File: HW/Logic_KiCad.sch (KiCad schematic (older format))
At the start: 32 parts, among them Q10 Q_NMOS_GSD, Q11 Q_NMOS_GSD, Q3 Q_NMOS_GSD, SW1 SW_SPDT, SW13 SW_SPST, SW14 SW_SPST, SW15 SW_SPST, U1 ESP32-PICO-D4

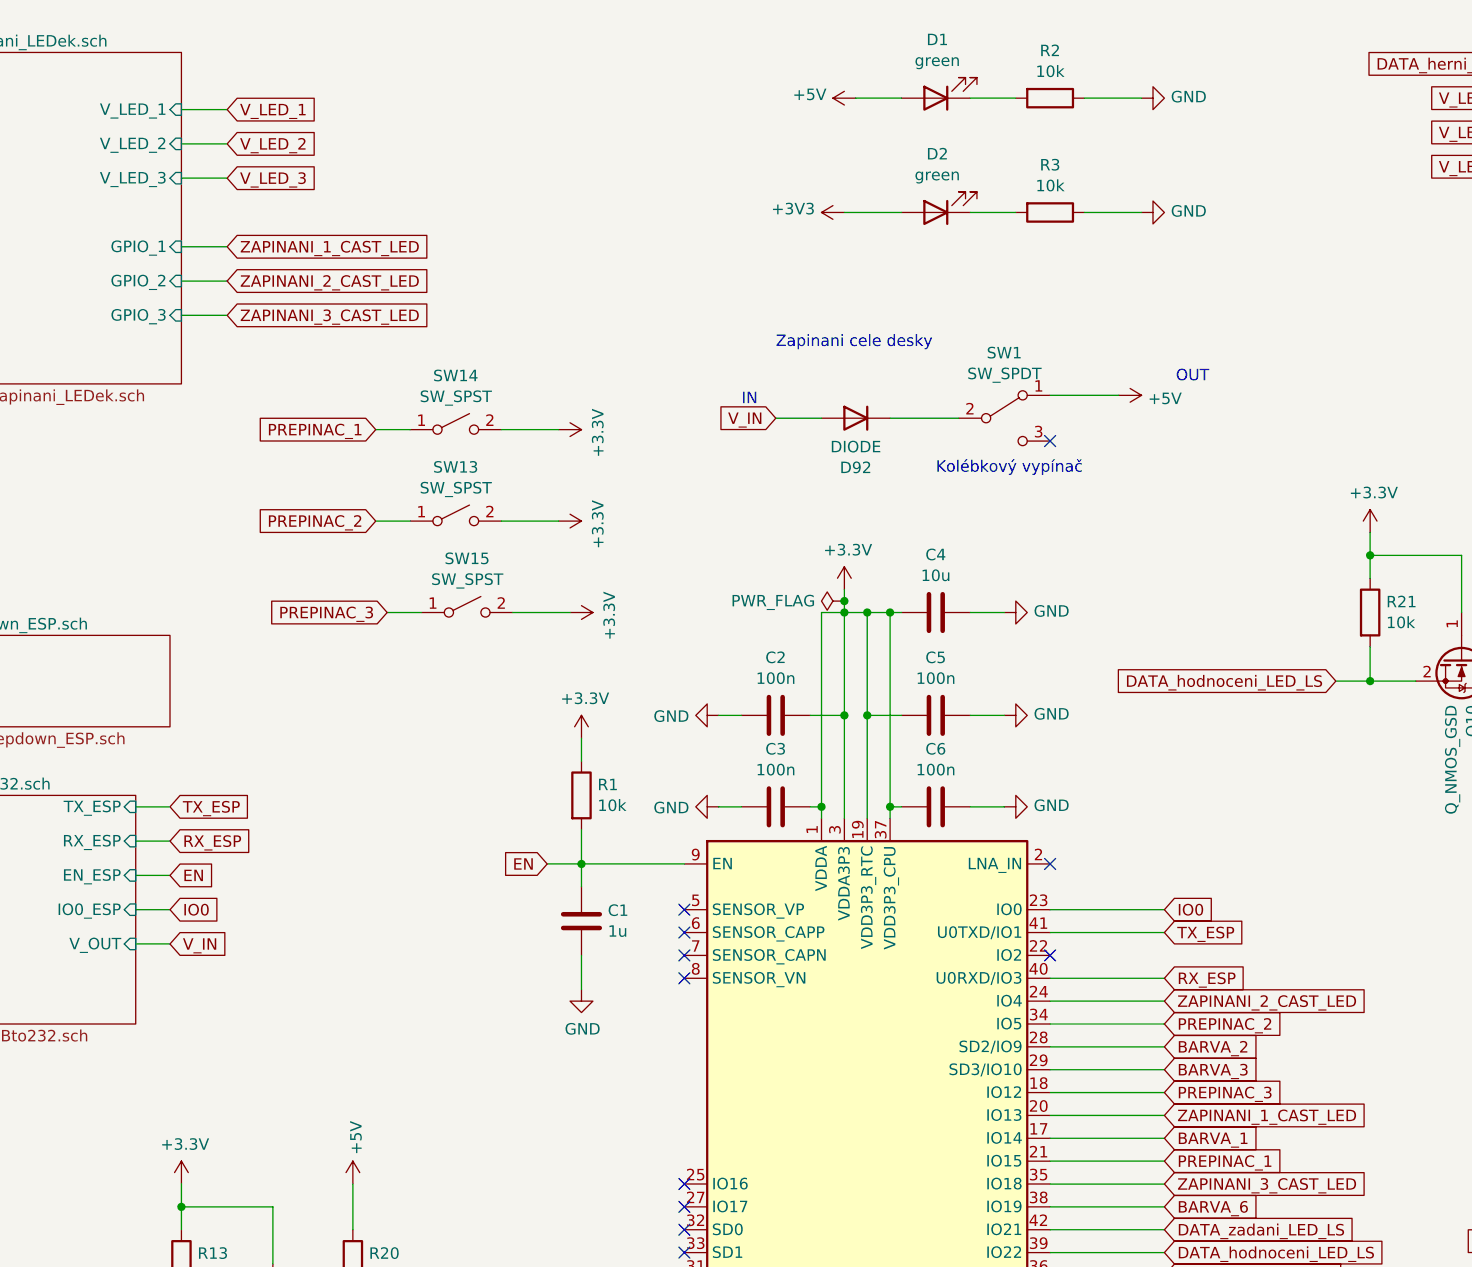
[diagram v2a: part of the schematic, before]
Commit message: repair DIPs, add pullup and pulldown resistors
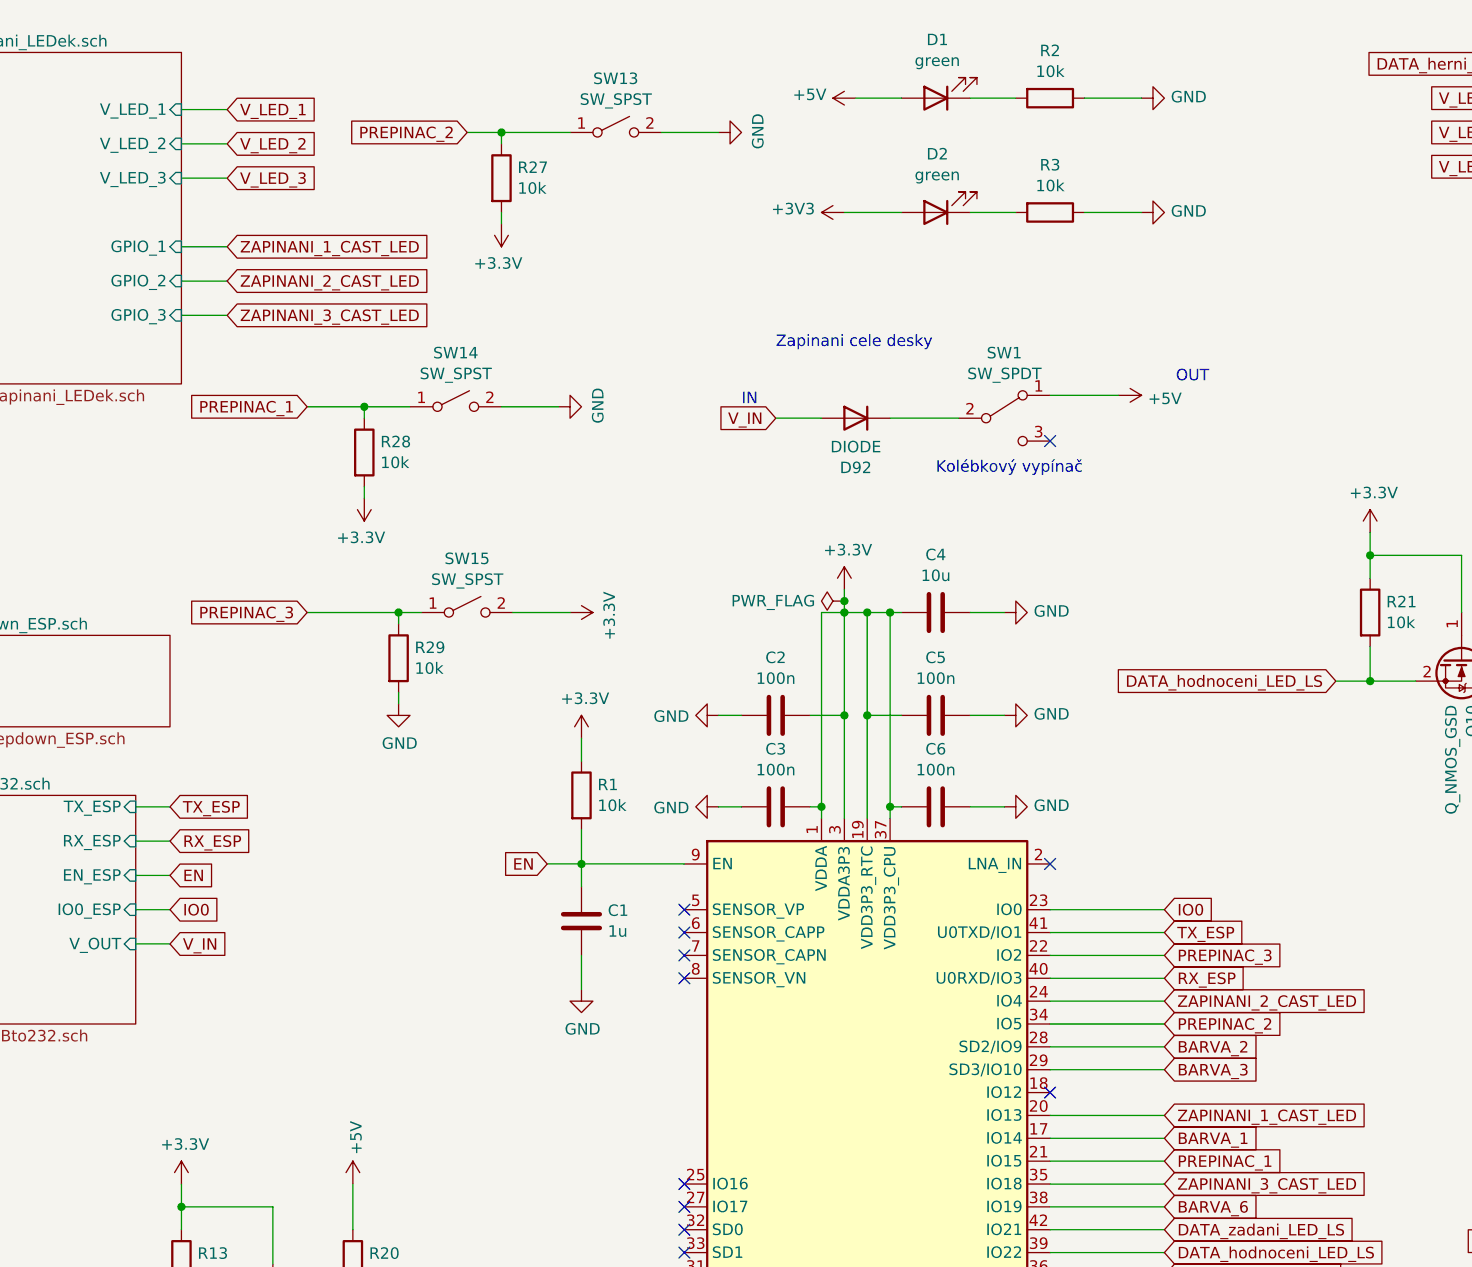
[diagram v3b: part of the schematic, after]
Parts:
- added R27, R28, R29: 10k, Resistor_SMD:R_0402_1005Metric, symbol Device:R
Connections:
- net +3V3: now also R27.2, R28.2; no longer SW13.2 (B), SW14.2 (B)
- net GND: now also SW13.2 (B), SW14.2 (B), R29.2
- net PREPINAC_1: now also R28.1
- net PREPINAC_2: now also R27.1
- net PREPINAC_3: now also U1.22 (IO2), R29.1; no longer U1.18 (IO12)
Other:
- moved on the sheet: SW13, SW14
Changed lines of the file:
@@
 L Switch:SW_SPST SW13
 U 1 1 603F7020
-P 2850 2750
-F 0 "SW13" H 2850 2985 50  0000 C CNN
-F 1 "SW_SPST" H 2850 2894 50  0000 C CNN
-F 2 "my_library:DIP1x1" H 2850 2750 50  0001 C CNN
-F 3 "~" H 2850 2750 50  0001 C CNN
-F 4 "0;0;0" H 2850 2750 50  0001 C CNN "JLCPCB_CORRECTION"
-F 5 "C54948" H 2850 2750 50  0001 C CNN "LCSC"
-	1    2850 2750
-	1    0    0    -1
-$EndComp
-Text GLabel 2500 2750 0    50   Input ~ 0
+P 3550 1050
+F 0 "SW13" H 3550 1285 50  0000 C CNN
+F 1 "SW_SPST" H 3550 1194 50  0000 C CNN
+F 2 "my_library:DIP1x1" H 3550 1050 50  0001 C CNN
+F 3 "~" H 3550 1050 50  0001 C CNN
+F 4 "0;0;0" H 3550 1050 50  0001 C CNN "JLCPCB_CORRECTION"
+F 5 "C54948" H 3550 1050 50  0001 C CNN "LCSC"
+	1    3550 1050
+	1    0    0    -1
+$EndComp
+Text GLabel 2900 1050 0    50   Input ~ 0
 PREPINAC_2
 Wire Wire Line
-	2650 2750 2500 2750
-Wire Wire Line
-	3300 2750 3050 2750
+	3350 1050 3050 1050
+Wire Wire Line
+	4000 1050 3750 1050
 $Comp
 L Switch:SW_SPST SW14
 U 1 1 604089F0
-P 2850 2350
-F 0 "SW14" H 2850 2585 50  0000 C CNN
-F 1 "SW_SPST" H 2850 2494 50  0000 C CNN
-F 2 "my_library:DIP1x1" H 2850 2350 50  0001 C CNN
-F 3 "~" H 2850 2350 50  0001 C CNN
-F 4 "0;0;0" H 2850 2350 50  0001 C CNN "JLCPCB_CORRECTION"
-F 5 "C54948" H 2850 2350 50  0001 C CNN "LCSC"
-	1    2850 2350
-	1    0    0    -1
-$EndComp
-Text GLabel 2500 2350 0    50   Input ~ 0
+P 2850 2250
+F 0 "SW14" H 2850 2485 50  0000 C CNN
+F 1 "SW_SPST" H 2850 2394 50  0000 C CNN
+F 2 "my_library:DIP1x1" H 2850 2250 50  0001 C CNN
+F 3 "~" H 2850 2250 50  0001 C CNN
+F 4 "0;0;0" H 2850 2250 50  0001 C CNN "JLCPCB_CORRECTION"
+F 5 "C54948" H 2850 2250 50  0001 C CNN "LCSC"
+	1    2850 2250
+	1    0    0    -1
+$EndComp
+Text GLabel 2200 2250 0    50   Input ~ 0
 PREPINAC_1
 Wire Wire Line
-	2650 2350 2500 2350
-Wire Wire Line
-	3300 2350 3050 2350
+	2650 2250 2450 2250
+Wire Wire Line
+	3300 2250 3050 2250
 Text GLabel 5950 4950 2    50   Input ~ 0
 PREPINAC_2
@@
 Wire Wire Line
 	5950 5550 5450 5550
-NoConn ~ 5450 4650
 Wire Wire Line
 	5950 4950 5450 4950
@@
 L power:+3.3V #PWR0224
 U 1 1 605155D5
-P 3300 2750
-F 0 "#PWR0224" H 3300 2600 50  0001 C CNN
-F 1 "+3.3V" H 3315 2923 50  0000 C CNN
-F 2 "" H 3300 2750 50  0001 C CNN
-F 3 "" H 3300 2750 50  0001 C CNN
-	1    3300 2750
-	0    1    1    0
-$EndComp
-Text GLabel 5950 5250 2    50   Input ~ 0
+P 3050 1450
+F 0 "#PWR0224" H 3050 1300 50  0001 C CNN
+F 1 "+3.3V" H 3065 1623 50  0000 C CNN
+F 2 "" H 3050 1450 50  0001 C CNN
+F 3 "" H 3050 1450 50  0001 C CNN
+	1    3050 1450
+	-1   0    0    1
+$EndComp
+Text GLabel 5950 4650 2    50   Input ~ 0
 PREPINAC_3
-Wire Wire Line
-	5450 5250 5950 5250
 $Comp
 L Switch:SW_SPST SW15
@@
 	1    0    0    -1
 $EndComp
-Text GLabel 2550 3150 0    50   Input ~ 0
+Text GLabel 2200 3150 0    50   Input ~ 0
 PREPINAC_3
 Wire Wire Line
-	2700 3150 2550 3150
+	2700 3150 2600 3150
 Wire Wire Line
 	3350 3150 3100 3150
@@
 L power:+3.3V #PWR0229
 U 1 1 6052B776
-P 3300 2350
-F 0 "#PWR0229" H 3300 2200 50  0001 C CNN
-F 1 "+3.3V" H 3315 2523 50  0000 C CNN
-F 2 "" H 3300 2350 50  0001 C CNN
-F 3 "" H 3300 2350 50  0001 C CNN
-	1    3300 2350
-	0    1    1    0
-$EndComp
+P 2450 2650
+F 0 "#PWR0229" H 2450 2500 50  0001 C CNN
+F 1 "+3.3V" H 2465 2823 50  0000 C CNN
+F 2 "" H 2450 2650 50  0001 C CNN
+F 3 "" H 2450 2650 50  0001 C CNN
+	1    2450 2650
+	-1   0    0    1
+$EndComp
+Wire Wire Line
+	5950 4650 5450 4650
+NoConn ~ 5450 5250
+$Comp
+L Device:R R28
+U 1 1 605389EB
+P 2450 2450
+F 0 "R28" H 2520 2496 50  0000 L CNN
+F 1 "10k" H 2520 2405 50  0000 L CNN
+F 2 "Resistor_SMD:R_0402_1005Metric" V 2380 2450 50  0001 C CNN
+F 3 "~" H 2450 2450 50  0001 C CNN
+F 4 "C25744" H 2450 2450 50  0001 C CNN "LCSC"
+F 5 "0;0;0" H 2450 2450 50  0001 C CNN "JLCPCB_CORRECTION"
+	1    2450 2450
+	1    0    0    -1
+$EndComp
+$Comp
+L Device:R R27
+U 1 1 60538DAC
+P 3050 1250
+F 0 "R27" H 3120 1296 50  0000 L CNN
+F 1 "10k" H 3120 1205 50  0000 L CNN
+F 2 "Resistor_SMD:R_0402_1005Metric" V 2980 1250 50  0001 C CNN
+F 3 "~" H 3050 1250 50  0001 C CNN
+F 4 "C25744" H 3050 1250 50  0001 C CNN "LCSC"
+F 5 "0;0;0" H 3050 1250 50  0001 C CNN "JLCPCB_CORRECTION"
+	1    3050 1250
+	1    0    0    -1
+$EndComp
+$Comp
+L Device:R R29
+U 1 1 605393EC
+P 2600 3350
+F 0 "R29" H 2670 3396 50  0000 L CNN
+F 1 "10k" H 2670 3305 50  0000 L CNN
+F 2 "Resistor_SMD:R_0402_1005Metric" V 2530 3350 50  0001 C CNN
+F 3 "~" H 2600 3350 50  0001 C CNN
+F 4 "C25744" H 2600 3350 50  0001 C CNN "LCSC"
+F 5 "0;0;0" H 2600 3350 50  0001 C CNN "JLCPCB_CORRECTION"
+	1    2600 3350
+	1    0    0    -1
+$EndComp
+$Comp
+L power:GND #PWR0230
+U 1 1 605398F0
+P 2600 3550
+F 0 "#PWR0230" H 2600 3300 50  0001 C CNN
+F 1 "GND" H 2605 3377 50  0000 C CNN
+F 2 "" H 2600 3550 50  0001 C CNN
+F 3 "" H 2600 3550 50  0001 C CNN
+	1    2600 3550
+	1    0    0    -1
+$EndComp
+$Comp
+L power:GND #PWR0231
+U 1 1 60539D13
+P 4000 1050
+F 0 "#PWR0231" H 4000 800 50  0001 C CNN
+F 1 "GND" H 4005 877 50  0000 C CNN
+F 2 "" H 4000 1050 50  0001 C CNN
+F 3 "" H 4000 1050 50  0001 C CNN
+	1    4000 1050
+	0    -1   -1   0
+$EndComp
+$Comp
+L power:GND #PWR0232
+U 1 1 60539F1B
+P 3300 2250
+F 0 "#PWR0232" H 3300 2000 50  0001 C CNN
+F 1 "GND" H 3305 2077 50  0000 C CNN
+F 2 "" H 3300 2250 50  0001 C CNN
+F 3 "" H 3300 2250 50  0001 C CNN
+	1    3300 2250
+	0    -1   -1   0
+$EndComp
+Wire Wire Line
+	2450 2300 2450 2250
+Connection ~ 2450 2250
+Wire Wire Line
+	2450 2250 2200 2250
+Wire Wire Line
+	3050 1100 3050 1050
+Connection ~ 3050 1050
+Wire Wire Line
+	3050 1050 2900 1050
+Wire Wire Line
+	2600 3200 2600 3150
+Connection ~ 2600 3150
+Wire Wire Line
+	2600 3150 2200 3150
+Wire Wire Line
+	2600 3500 2600 3550
+Wire Wire Line
+	3050 1450 3050 1400
+Wire Wire Line
+	2450 2650 2450 2600
 $EndSCHEMATC

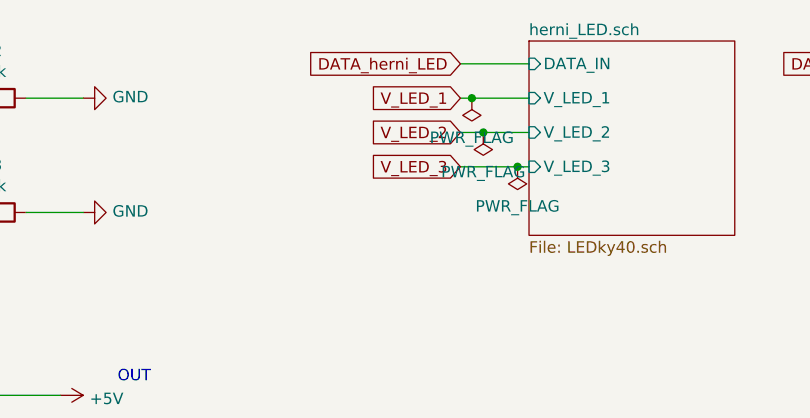
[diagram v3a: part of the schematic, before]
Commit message: add tooling holes
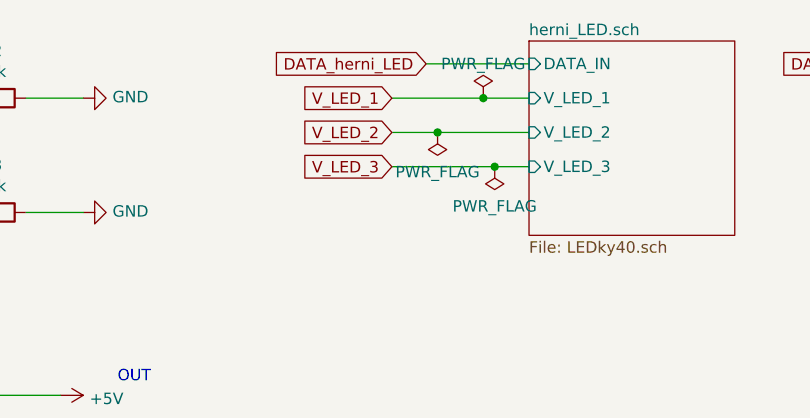
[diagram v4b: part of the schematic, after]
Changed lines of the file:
@@
 Comment4 ""
 $EndDescr
-Text GLabel 7500 750  0    50   Input ~ 0
+Text GLabel 7350 750  0    50   Input ~ 0
 DATA_herni_LED
 Text GLabel 9750 750  0    50   Input ~ 0
@@
 Text GLabel 9750 900  0    50   Input ~ 0
 V_LED_1
-Text GLabel 7500 900  0    50   Input ~ 0
+Text GLabel 7200 900  0    50   Input ~ 0
 V_LED_1
-Text GLabel 7500 1050 0    50   Input ~ 0
+Text GLabel 7200 1050 0    50   Input ~ 0
 V_LED_2
 Wire Wire Line
-	7500 750  7800 750
-Wire Wire Line
-	7500 900  7550 900
+	7350 750  7800 750
+Wire Wire Line
+	7800 900  7600 900
 Text GLabel 5950 5350 2    50   Input ~ 0
 ZAPINANI_1_CAST_LED
@@
 	5800 7350 5800 7150
 Wire Wire Line
-	7800 1200 7750 1200
-Text GLabel 7500 1200 0    50   Input ~ 0
+	7800 1200 7650 1200
+Text GLabel 7200 1200 0    50   Input ~ 0
 V_LED_3
 Text GLabel 9750 1200 0    50   Input ~ 0
@@
 L power:PWR_FLAG #FLG0105
 U 1 1 6051C980
-P 7600 1050
-F 0 "#FLG0105" H 7600 1125 50  0001 C CNN
-F 1 "PWR_FLAG" H 7600 1223 50  0000 C CNN
-F 2 "" H 7600 1050 50  0001 C CNN
-F 3 "~" H 7600 1050 50  0001 C CNN
-	1    7600 1050
+P 7400 1050
+F 0 "#FLG0105" H 7400 1125 50  0001 C CNN
+F 1 "PWR_FLAG" H 7400 1223 50  0000 C CNN
+F 2 "" H 7400 1050 50  0001 C CNN
+F 3 "~" H 7400 1050 50  0001 C CNN
+	1    7400 1050
 	-1   0    0    1
 $EndComp
@@
 L power:PWR_FLAG #FLG0107
 U 1 1 6051CE63
-P 7750 1200
-F 0 "#FLG0107" H 7750 1275 50  0001 C CNN
-F 1 "PWR_FLAG" H 7750 1373 50  0000 C CNN
-F 2 "" H 7750 1200 50  0001 C CNN
-F 3 "~" H 7750 1200 50  0001 C CNN
-	1    7750 1200
+P 7650 1200
+F 0 "#FLG0107" H 7650 1275 50  0001 C CNN
+F 1 "PWR_FLAG" H 7650 1373 50  0000 C CNN
+F 2 "" H 7650 1200 50  0001 C CNN
+F 3 "~" H 7650 1200 50  0001 C CNN
+	1    7650 1200
 	-1   0    0    1
 $EndComp
-Connection ~ 7750 1200
-Wire Wire Line
-	7750 1200 7500 1200
+Connection ~ 7650 1200
+Wire Wire Line
+	7650 1200 7200 1200
 $Comp
 L power:PWR_FLAG #FLG0109
 U 1 1 6051D33A
-P 7550 900
-F 0 "#FLG0109" H 7550 975 50  0001 C CNN
-F 1 "PWR_FLAG" H 7550 1073 50  0000 C CNN
-F 2 "" H 7550 900 50  0001 C CNN
-F 3 "~" H 7550 900 50  0001 C CNN
-	1    7550 900
-	-1   0    0    1
-$EndComp
-Connection ~ 7550 900
-Wire Wire Line
-	7550 900  7800 900
+P 7600 900
+F 0 "#FLG0109" H 7600 975 50  0001 C CNN
+F 1 "PWR_FLAG" H 7600 1050 50  0000 C CNN
+F 2 "" H 7600 900 50  0001 C CNN
+F 3 "~" H 7600 900 50  0001 C CNN
+	1    7600 900
+	1    0    0    -1
+$EndComp
+Connection ~ 7600 900
+Wire Wire Line
+	7600 900  7200 900
 Wire Wire Line
 	9750 900  9950 900
@@
 	9750 1200 9950 1200
 Wire Wire Line
-	7500 1050 7600 1050
+	7200 1050 7400 1050
 Wire Wire Line
 	9800 2150 9950 2150
-Connection ~ 7600 1050
-Wire Wire Line
-	7600 1050 7800 1050
+Connection ~ 7400 1050
+Wire Wire Line
+	7400 1050 7800 1050
 Wire Wire Line
 	9750 1050 9950 1050

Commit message: update rotation of components for fab, update folder fab
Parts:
- D92: JLCPCB_CORRECTION 0;0;180 -> 0;0;0
- SW13: JLCPCB_CORRECTION 0;0;0 -> 0;0;270
- SW14, SW15: JLCPCB_CORRECTION 0;0;0 -> 0;0;90
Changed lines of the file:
@@
 F 5 "D" H 4600 2300 50  0001 L CNN "Spice_Primitive"
 F 6 "C8678" H 4600 2300 50  0001 C CNN "LCSC"
-F 7 "0;0;180" H 4600 2300 50  0001 C CNN "JLCPCB_CORRECTION"
+F 7 "0;0;0" H 4600 2300 50  0001 C CNN "JLCPCB_CORRECTION"
 	1    4600 2300
 	-1   0    0    -1
@@
 F 2 "my_library:DIP1x1" H 3550 1050 50  0001 C CNN
 F 3 "~" H 3550 1050 50  0001 C CNN
-F 4 "0;0;0" H 3550 1050 50  0001 C CNN "JLCPCB_CORRECTION"
+F 4 "0;0;270" H 3550 1050 50  0001 C CNN "JLCPCB_CORRECTION"
 F 5 "C54948" H 3550 1050 50  0001 C CNN "LCSC"
 	1    3550 1050
@@
 F 2 "my_library:DIP1x1" H 2850 2250 50  0001 C CNN
 F 3 "~" H 2850 2250 50  0001 C CNN
-F 4 "0;0;0" H 2850 2250 50  0001 C CNN "JLCPCB_CORRECTION"
+F 4 "0;0;90" H 2850 2250 50  0001 C CNN "JLCPCB_CORRECTION"
 F 5 "C54948" H 2850 2250 50  0001 C CNN "LCSC"
 	1    2850 2250
@@
 F 2 "my_library:DIP1x1" H 2900 3150 50  0001 C CNN
 F 3 "~" H 2900 3150 50  0001 C CNN
-F 4 "0;0;0" H 2900 3150 50  0001 C CNN "JLCPCB_CORRECTION"
+F 4 "0;0;90" H 2900 3150 50  0001 C CNN "JLCPCB_CORRECTION"
 F 5 "C54948" H 2900 3150 50  0001 C CNN "LCSC"
 	1    2900 3150

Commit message: Version 1.2 for fab
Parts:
- C1: value 1u -> H
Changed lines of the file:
@@
 P 3400 4500
 F 0 "C1" H 3285 4454 50  0000 R CNN
-F 1 "1u" H 3285 4545 50  0000 R CNN
+F 1 "H" H 3285 4545 50  0000 R CNN
 F 2 "Capacitor_SMD:C_0402_1005Metric" H 3438 4350 50  0001 C CNN
 F 3 "~" H 3400 4500 50  0001 C CNN
